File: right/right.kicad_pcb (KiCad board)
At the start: 2 copper layers, 117.6 x 97.9 mm, 53 parts, among them J2 USB_C_Receptacle_OUT, SW1 SW_Push, SW2 SW_SPDT, U1 STM32G0B1CBTx, U2 SRV05-4, U3 XC6206P332MR, U4 FSUSB42MUX

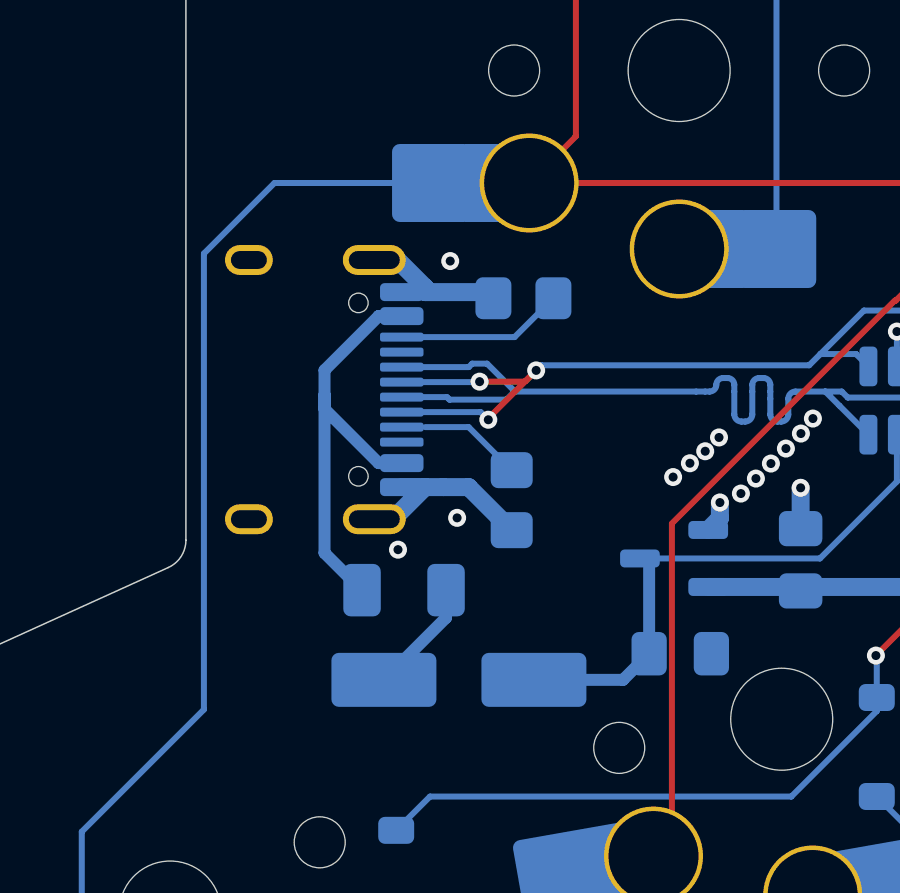
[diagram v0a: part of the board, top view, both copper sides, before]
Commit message: added 3d models and moved the usb port a bit on right
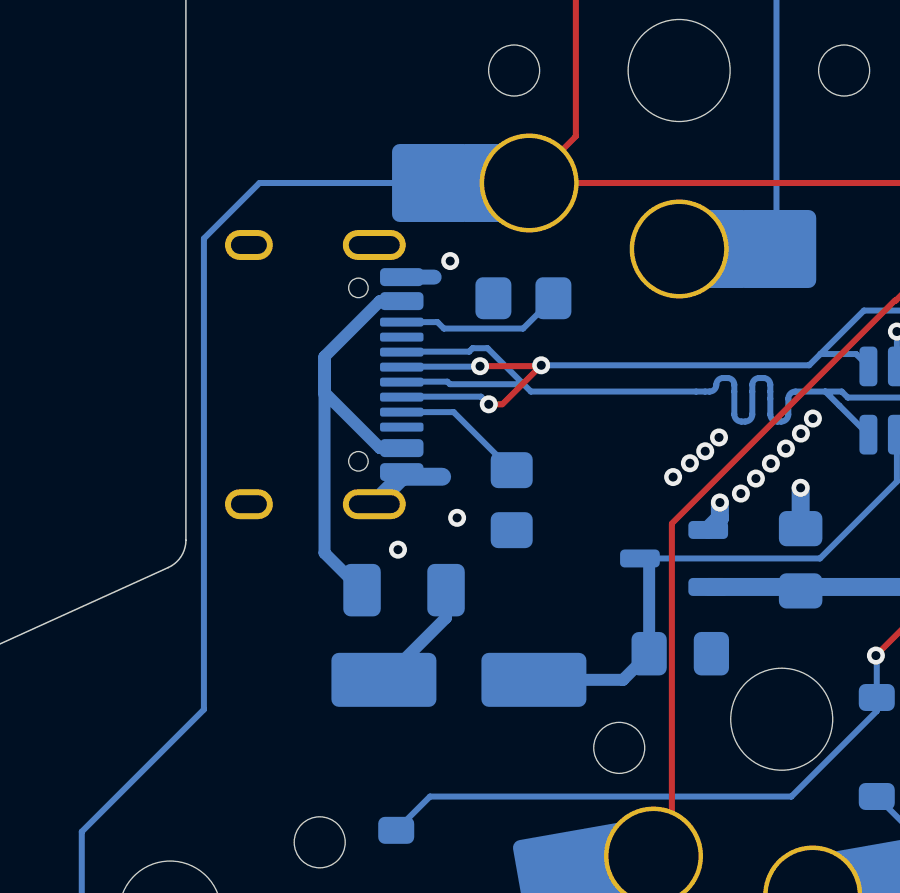
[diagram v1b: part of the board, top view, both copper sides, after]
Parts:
- KEY1, KEY10, KEY11, KEY12, KEY13, KEY14, KEY15, KEY16, KEY17, KEY2, KEY3, KEY4, KEY5, KEY6, KEY7, KEY8, KEY9: footprint marbastlib-choc:SW_choc_v1_HS_CPG135001S30_1u -> Keyswitches Marbastlib Choc:SW_choc_v1_HS_CPG135001S30_1u
- moved J2 0.50 mm to (76.0, 117.5)
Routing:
- net GND: track 15.4 -> 10.00 mm
- net Net-(J2-CC1): track 3.48 -> 4.47 mm

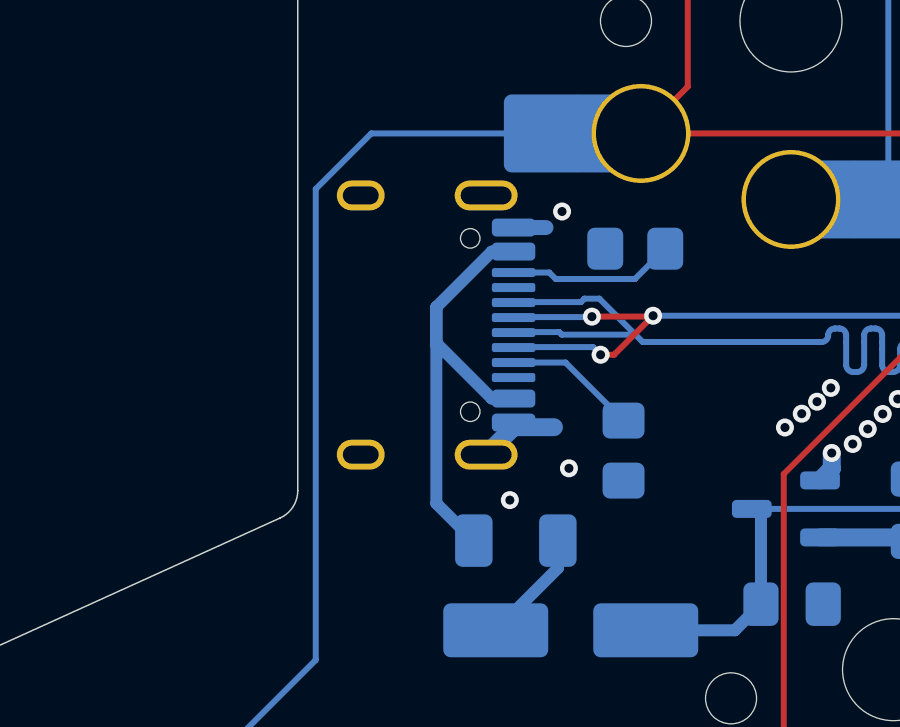
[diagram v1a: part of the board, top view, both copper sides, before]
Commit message: tweaked right usb a lot, hopefully this is it; waiting for screws
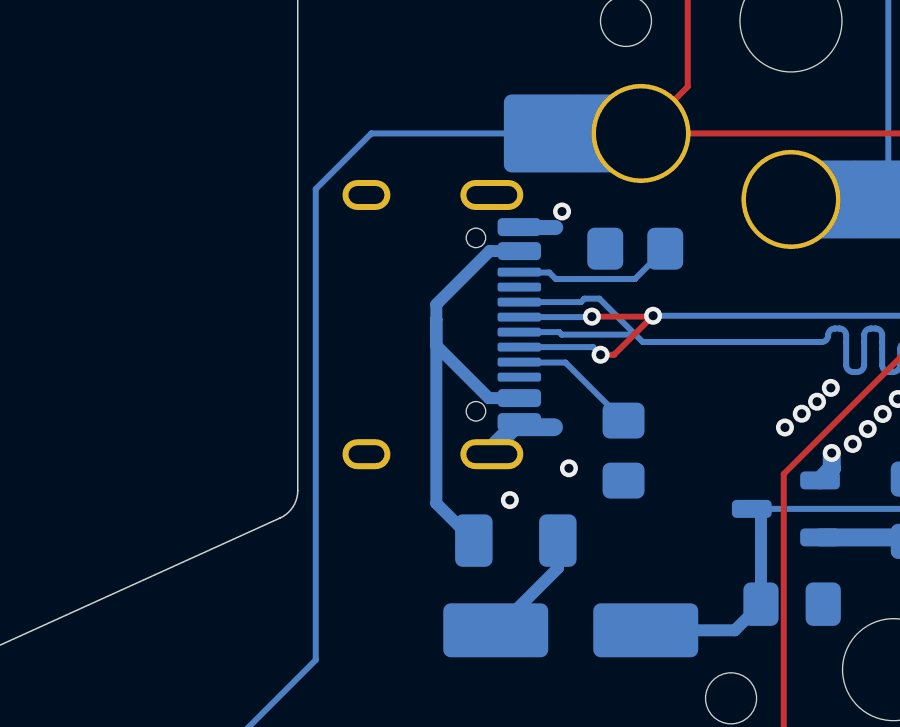
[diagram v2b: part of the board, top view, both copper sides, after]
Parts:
- moved J2 0.19 mm to (76.2, 117.5)
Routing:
- net VBUS: track 16.2 -> 17.1 mm
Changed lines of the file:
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@@
 		(fp_arc
 			(start 6.45 -6.125)
-			(mid 7.015685 -5.890686)
+			(mid 7.015684 -5.890686)
 			(end 7.25 -5.325)
 			(stroke
@@
 		(fp_arc
 			(start 6.45 -6.125)
-			(mid 7.015685 -5.890686)
+			(mid 7.015684 -5.890686)
 			(end 7.25 -5.325)
 			(stroke
@@
 	(footprint "Connector_USB:USB_C_Receptacle_HRO_TYPE-C-31-M-12"
 		(layer "B.Cu")
-		(at 76.05 117.535 90)
+		(at 76.24 117.52 90)
 		(descr "USB Type-C receptacle for USB 2.0 and PD, http://www.krhro.com/uploads/soft/180320/1-1P320120243.pdf")
 		(tags "usb usb-c 2.0 pd")
@@
 	)
 	(segment
-		(start 80.095 114.285)
-		(end 81.175 114.285)
+		(start 80.42 114.285)
+		(end 81.5 114.285)
 		(width 0.5)
 		(layer "B.Cu")
@@
 	)
 	(segment
-		(start 78.76 124.72)
-		(end 78.77 124.72)
+		(start 77.52 117.34617)
+		(end 77.52 118.219999)
 		(width 0.4)
 		(layer "B.Cu")
@@
 	)
 	(segment
-		(start 79.370001 115.085)
-		(end 80.095 115.085)
+		(start 80.495 119.97)
+		(end 79.770001 119.97)
 		(width 0.4)
 		(layer "B.Cu")
@@
 	)
 	(segment
-		(start 77.52 116.935001)
-		(end 77.52 118.134999)
+		(start 77.52 117.34617)
+		(end 77.52 116.84617)
 		(width 0.4)
 		(layer "B.Cu")
@@
 	)
 	(segment
-		(start 79.370001 119.985)
-		(end 80.095 119.985)
+		(start 79.29617 115.07)
+		(end 79.995 115.07)
 		(width 0.4)
 		(layer "B.Cu")
@@
 	)
 	(segment
-		(start 77.52 118.21)
-		(end 77.52 123.48)
+		(start 79.79617 115.07)
+		(end 80.495 115.07)
 		(width 0.4)
 		(layer "B.Cu")
@@
 	)
 	(segment
-		(start 77.52 118.21)
-		(end 77.52 116.935001)
+		(start 77.52 123.48)
+		(end 77.52 117.34617)
 		(width 0.4)
 		(layer "B.Cu")
@@
 	)
 	(segment
-		(start 77.52 116.935001)
-		(end 79.370001 115.085)
+		(start 78.76 124.72)
+		(end 77.52 123.48)
 		(width 0.4)
 		(layer "B.Cu")
@@
 	)
 	(segment
-		(start 77.52 118.134999)
-		(end 79.370001 119.985)
+		(start 77.52 116.84617)
+		(end 79.29617 115.07)
 		(width 0.4)
 		(layer "B.Cu")
@@
 	)
 	(segment
-		(start 77.52 123.48)
+		(start 77.52 118.219999)
+		(end 79.270001 119.97)
+		(width 0.4)
+		(layer "B.Cu")
+		(net "VBUS")
+	)
+	(segment
+		(start 78.77 124.72)
 		(end 78.76 124.72)
 		(width 0.4)
 		(layer "B.Cu")
+		(net "VBUS")
+	)
+	(segment
+		(start 79.270001 119.97)
+		(end 79.995 119.97)
+		(width 0.4)
+		(layer "B.Cu")
